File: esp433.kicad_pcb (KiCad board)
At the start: 2 copper layers, 47.1 x 72.6 mm, 35 parts, among them J1 USB_OTG, J2 CONN_01X03, Q1 MBT2222ADW1T1, SW1 SW_Push, U1 AP2127K-3.3, U2 IRM-02-5, U3 ESP-12E, U4 FT231XS

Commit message: Add rf circuit
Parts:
- added AE1: Antenna, esp433:W3127, F.Cu at (97.7, 130.3)
- added C3: 100n, Capacitors_SMD:C_0603, F.Cu at (102.1, 117.9)
- added C4: 220p, Capacitors_SMD:C_0603, F.Cu at (100.8, 117.9)
- added C5: 680p, Capacitors_SMD:C_0603, F.Cu at (99.6, 117.9)
- added C6: 12p, Capacitors_SMD:C_0603, F.Cu at (98.8, 125.2)
- added C7: 12p, Capacitors_SMD:C_0603, F.Cu at (97.3, 121.4)
- added C8: 100n, Capacitors_SMD:C_0603, F.Cu at (103.6, 124.5)
- added L2: 27nH, Inductors_SMD:L_0603, F.Cu at (98.0, 119.4)
- added L3: 15nH, Inductors_SMD:L_0603, F.Cu at (98.0, 123.4)
- added R6: R_Variable, Potentiometers:Potentiometer_Trimmer_Vishay_TS53YL, F.Cu at (108.2, 121.4)
- added U3: MAX7044, TO_SOT_Packages_SMD:SOT-23-8, F.Cu at (102.4, 121.4)
- added Y1: Crystal, Crystals:Crystal_HC49-U_Vertical, F.Cu at (117.3, 117.8)
- SW1: footprint Buttons_Switches_SMD:SW_SPST_PTS645 -> Buttons_Switches_SMD:SW_SPST_B3U-1000P
- moved SW1 37.5 mm to (135.6, 84.6), turned to 270 degrees
- moved D1 11.9 mm to (128.0, 120.4)
- moved J2 3.54 mm to (130.6, 129.3)
- renumbered C7 to C1, C2 to C10, C3 to C11, C4 to C12, C5 to C13, C6 to C14, C8 to C2, C1 to C9, R9 to R10, R10 to R11, R6 to R7, R7 to R9, U2 to U1, U1 to U2, U3 to U4, U4 to U5
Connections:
- U4 pad 5: (no net) -> /RF_CLK
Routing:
- net /RF_CLK: track 0.00 -> 36.9 mm, vias 0 -> 2
- net /RF_MOD: track 44.7 -> 73.9 mm, vias 0 -> 2
- net GND: track 26.8 -> 47.1 mm, vias 13 -> 21
- net +3V3: track 7.55 -> 24.9 mm, vias 3 -> 5
- net Net-(U3-Pad8): track 0.00 -> 16.0 mm
- net Net-(U3-Pad1): track 0.00 -> 15.8 mm
- net Net-(D1-Pad2): track 15.0 -> 27.9 mm
- net Net-(C3-Pad1): track 0.00 -> 10.2 mm
- net Net-(AE1-Pad1): track 0.00 -> 6.28 mm
- net Net-(C7-Pad1): track 0.00 -> 5.99 mm
- net +5V: track 45.2 -> 39.9 mm
- net /RESET: track 47.9 -> 49.8 mm, vias 4 -> 2

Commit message: Rearrange silk
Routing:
- net GND: track 47.1 -> 46.1 mm

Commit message: Rearrange filtering according to datasheet
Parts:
- moved C3 1.08 mm to (102.9, 117.1), turned to 180 degrees
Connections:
- C3 pad 1: Net-(C3-Pad1) -> +3V3
- C4 pad 1: Net-(C3-Pad1) -> Net-(C4-Pad1)
- C5 pad 1: Net-(C3-Pad1) -> Net-(C4-Pad1)
- L2 pad 1: Net-(C3-Pad1) -> Net-(C4-Pad1)
- R6 pad 2: Net-(C3-Pad1) -> Net-(C4-Pad1)
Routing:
- net +3V3: track 24.9 -> 14.0 mm
- net Net-(C4-Pad1): track 0.00 -> 10.2 mm
- net Net-(C3-Pad1): track 10.2 -> 0.00 mm
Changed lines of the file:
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@@
   (general
     (links 90)
-    (no_connects 0)
+    (no_connects 2)
     (area 90.679199 65.202999 137.920801 137.997001)
     (thickness 1.6)
     (drawings 20)
-    (tracks 319)
+    (tracks 317)
     (zones 0)
     (modules 47)
@@
   (net 23 /AC-L)
   (net 24 "Net-(AE1-Pad1)")
-  (net 25 "Net-(C3-Pad1)")
+  (net 25 "Net-(C4-Pad1)")
   (net 26 "Net-(C7-Pad1)")
   (net 27 "Net-(C9-Pad1)")
@@
     (add_net "Net-(AE1-Pad1)")
     (add_net "Net-(C14-Pad1)")
-    (add_net "Net-(C3-Pad1)")
+    (add_net "Net-(C4-Pad1)")
     (add_net "Net-(C7-Pad1)")
     (add_net "Net-(C9-Pad1)")
@@
   )
   (module Capacitors_SMD:C_0603 (layer F.Cu)
-    (at 102.108 117.856 90)
+    (at 102.87 117.094 180)
     (descr "Capacitor SMD 0603, reflow soldering, AVX (see smccp.pdf)")
     (tags "capacitor 0603")
     (attr smd)
-    (fp_text reference C3 (at 0.508 3.81 90) (layer F.SilkS)
-      (effects (font (size 1 1) (thickness 0.15)))
-    )
-    (fp_text value 100n (at 0 1.5 90) (layer F.Fab)
+    (fp_text reference C3 (at -2.286 0 180) (layer F.SilkS)
+      (effects (font (size 1 1) (thickness 0.15)))
+    )
+    (fp_text value 100n (at 0 1.5 180) (layer F.Fab)
+      (effects (font (size 1 1) (thickness 0.15)))
+    )
+    (fp_line (start 1.4 0.65) (end -1.4 0.65) (layer F.CrtYd) (width 0.05))
+    (fp_line (start 1.4 0.65) (end 1.4 -0.65) (layer F.CrtYd) (width 0.05))
+    (fp_line (start -1.4 -0.65) (end -1.4 0.65) (layer F.CrtYd) (width 0.05))
+    (fp_line (start -1.4 -0.65) (end 1.4 -0.65) (layer F.CrtYd) (width 0.05))
+    (fp_line (start 0.35 0.6) (end -0.35 0.6) (layer F.SilkS) (width 0.12))
+    (fp_line (start -0.35 -0.6) (end 0.35 -0.6) (layer F.SilkS) (width 0.12))
+    (fp_line (start -0.8 -0.4) (end 0.8 -0.4) (layer F.Fab) (width 0.1))
+    (fp_line (start 0.8 -0.4) (end 0.8 0.4) (layer F.Fab) (width 0.1))
+    (fp_line (start 0.8 0.4) (end -0.8 0.4) (layer F.Fab) (width 0.1))
+    (fp_line (start -0.8 0.4) (end -0.8 -0.4) (layer F.Fab) (width 0.1))
+    (fp_text user %R (at 0 0 180) (layer F.Fab)
+      (effects (font (size 0.3 0.3) (thickness 0.075)))
+    )
+    (pad 2 smd rect (at 0.75 0 180) (size 0.8 0.75) (layers F.Cu F.Paste F.Mask)
+      (net 1 GND))
+    (pad 1 smd rect (at -0.75 0 180) (size 0.8 0.75) (layers F.Cu F.Paste F.Mask)
+      (net 6 +3V3))
+    (model Capacitors_SMD.3dshapes/C_0603.wrl
+      (at (xyz 0 0 0))
+      (scale (xyz 1 1 1))
+      (rotate (xyz 0 0 0))
+    )
+  )
+  (module Capacitors_SMD:C_0603 (layer F.Cu)
+    (at 100.838 117.856 90)
+    (descr "Capacitor SMD 0603, reflow soldering, AVX (see smccp.pdf)")
+    (tags "capacitor 0603")
+    (attr smd)
+    (fp_text reference C4 (at -0.762 1.27 90) (layer F.SilkS)
+      (effects (font (size 1 1) (thickness 0.15)))
+    )
+    (fp_text value 220p (at 0 1.5 90) (layer F.Fab)
       (effects (font (size 1 1) (thickness 0.15)))
     )
@@
       (net 1 GND))
     (pad 1 smd rect (at -0.75 0 90) (size 0.8 0.75) (layers F.Cu F.Paste F.Mask)
-      (net 25 "Net-(C3-Pad1)"))
+      (net 25 "Net-(C4-Pad1)"))
     (model Capacitors_SMD.3dshapes/C_0603.wrl
       (at (xyz 0 0 0))
@@
   )
   (module Capacitors_SMD:C_0603 (layer F.Cu)
-    (at 100.838 117.856 90)
+    (at 99.568 117.856 90)
     (descr "Capacitor SMD 0603, reflow soldering, AVX (see smccp.pdf)")
     (tags "capacitor 0603")
     (attr smd)
-    (fp_text reference C4 (at 0.508 3.81 90) (layer F.SilkS)
-      (effects (font (size 1 1) (thickness 0.15)))
-    )
-    (fp_text value 220p (at 0 1.5 90) (layer F.Fab)
+    (fp_text reference C5 (at 0.508 -1.524 270) (layer F.SilkS)
+      (effects (font (size 1 1) (thickness 0.15)))
+    )
+    (fp_text value 680p (at 0 1.5 90) (layer F.Fab)
       (effects (font (size 1 1) (thickness 0.15)))
     )
@@
       (net 1 GND))
     (pad 1 smd rect (at -0.75 0 90) (size 0.8 0.75) (layers F.Cu F.Paste F.Mask)
-      (net 25 "Net-(C3-Pad1)"))
-    (model Capacitors_SMD.3dshapes/C_0603.wrl
-      (at (xyz 0 0 0))
-      (scale (xyz 1 1 1))
-      (rotate (xyz 0 0 0))
-    )
-  )
-  (module Capacitors_SMD:C_0603 (layer F.Cu)
-    (at 99.568 117.856 90)
-    (descr "Capacitor SMD 0603, reflow soldering, AVX (see smccp.pdf)")
-    (tags "capacitor 0603")
-    (attr smd)
-    (fp_text reference C5 (at 0.508 3.81 90) (layer F.SilkS)
-      (effects (font (size 1 1) (thickness 0.15)))
-    )
-    (fp_text value 680p (at 0 1.5 90) (layer F.Fab)
-      (effects (font (size 1 1) (thickness 0.15)))
-    )
-    (fp_line (start 1.4 0.65) (end -1.4 0.65) (layer F.CrtYd) (width 0.05))
-    (fp_line (start 1.4 0.65) (end 1.4 -0.65) (layer F.CrtYd) (width 0.05))
-    (fp_line (start -1.4 -0.65) (end -1.4 0.65) (layer F.CrtYd) (width 0.05))
-    (fp_line (start -1.4 -0.65) (end 1.4 -0.65) (layer F.CrtYd) (width 0.05))
-    (fp_line (start 0.35 0.6) (end -0.35 0.6) (layer F.SilkS) (width 0.12))
-    (fp_line (start -0.35 -0.6) (end 0.35 -0.6) (layer F.SilkS) (width 0.12))
-    (fp_line (start -0.8 -0.4) (end 0.8 -0.4) (layer F.Fab) (width 0.1))
-    (fp_line (start 0.8 -0.4) (end 0.8 0.4) (layer F.Fab) (width 0.1))
-    (fp_line (start 0.8 0.4) (end -0.8 0.4) (layer F.Fab) (width 0.1))
-    (fp_line (start -0.8 0.4) (end -0.8 -0.4) (layer F.Fab) (width 0.1))
-    (fp_text user %R (at 0 0 90) (layer F.Fab)
-      (effects (font (size 0.3 0.3) (thickness 0.075)))
-    )
-    (pad 2 smd rect (at 0.75 0 90) (size 0.8 0.75) (layers F.Cu F.Paste F.Mask)
-      (net 1 GND))
-    (pad 1 smd rect (at -0.75 0 90) (size 0.8 0.75) (layers F.Cu F.Paste F.Mask)
-      (net 25 "Net-(C3-Pad1)"))
+      (net 25 "Net-(C4-Pad1)"))
     (model Capacitors_SMD.3dshapes/C_0603.wrl
       (at (xyz 0 0 0))
@@
     (fp_line (start -0.5 -0.68) (end 0.5 -0.68) (layer F.SilkS) (width 0.12))
     (pad 1 smd rect (at -0.75 0 270) (size 0.5 0.9) (layers F.Cu F.Paste F.Mask)
-      (net 25 "Net-(C3-Pad1)"))
+      (net 25 "Net-(C4-Pad1)"))
     (pad 2 smd rect (at 0.75 0 270) (size 0.5 0.9) (layers F.Cu F.Paste F.Mask)
       (net 26 "Net-(C7-Pad1)"))
@@
       (net 6 +3V3))
     (pad 2 smd rect (at -2.75 0 270) (size 2 1.3) (layers F.Cu F.Mask)
-      (net 25 "Net-(C3-Pad1)"))
+      (net 25 "Net-(C4-Pad1)"))
     (pad 3 smd rect (at 2.75 1.15 270) (size 1.3 1.3) (layers F.Cu F.Mask))
     (model Potentiometers.3dshapes/Potentiometer_Trimmer_Vishay_TS53YL.wrl
@@
   (segment (start 125.222 120.396) (end 127.166 120.396) (width 0.508) (layer F.Cu) (net 5))
   (segment (start 121.158 116.332) (end 125.222 120.396) (width 0.508) (layer B.Cu) (net 5))
-  (segment (start 102.858 113.03) (end 102.596 113.03) (width 0.25) (layer F.Cu) (net 5))
-  (segment (start 102.907 124.46) (end 105.193 122.174) (width 0.25) (layer F.Cu) (net 6))
-  (segment (start 105.193 122.174) (end 113.284 122.174) (width 0.25) (layer F.Cu) (net 6))
-  (via (at 113.284 122.174) (size 0.6) (drill 0.4) (layers F.Cu B.Cu) (net 6))
-  (segment (start 109.354 124.118) (end 113.196 124.118) (width 0.34798) (layer F.Cu) (net 6))
-  (via (at 113.284 124.206) (size 0.6) (drill 0.4) (layers F.Cu B.Cu) (net 6))
-  (segment (start 113.196 124.118) (end 113.284 124.206) (width 0.34798) (layer F.Cu) (net 6))
+  (segment (start 102.907 124.46) (end 104.431 122.936) (width 0.25) (layer F.Cu) (net 6))
+  (segment (start 104.431 122.936) (end 105.156 122.936) (width 0.25) (layer F.Cu) (net 6))
+  (via (at 105.156 122.936) (size 0.6) (drill 0.4) (layers F.Cu B.Cu) (net 6))
+  (segment (start 103.62 117.094) (end 105.156 117.094) (width 0.34798) (layer F.Cu) (net 6))
+  (via (at 105.156 117.094) (size 0.6) (drill 0.4) (layers F.Cu B.Cu) (net 6))
   (segment (start 102.882 124.46) (end 102.907 124.46) (width 0.25) (layer F.Cu) (net 6))
   (segment (start 102.692 122.512) (end 102.692 124.27) (width 0.25) (layer F.Cu) (net 6))
@@
   (segment (start 98.044 124.194) (end 98.044 125.21) (width 0.25) (layer F.Cu) (net 24))
   (segment (start 98.044 125.21) (end 98.056 125.222) (width 0.25) (layer F.Cu) (net 24))
-  (segment (start 102.108 118.606) (end 108.192 118.606) (width 0.34798) (layer F.Cu) (net 25))
+  (segment (start 108.204 118.618) (end 100.85 118.618) (width 0.34798) (layer F.Cu) (net 25))
+  (segment (start 100.85 118.618) (end 100.838 118.606) (width 0.25) (layer F.Cu) (net 25))
   (segment (start 108.192 118.606) (end 108.204 118.618) (width 0.25) (layer F.Cu) (net 25))
-  (segment (start 100.838 118.606) (end 102.108 118.606) (width 0.34798) (layer F.Cu) (net 25))
   (segment (start 99.568 118.606) (end 100.838 118.606) (width 0.34798) (layer F.Cu) (net 25))
   (segment (start 98.044 118.63) (end 99.544 118.63) (width 0.34798) (layer F.Cu) (net 25))
@@
     (polygon
       (pts
-        (xy 112.776 91.694) (xy 137.922 91.694) (xy 137.922 125.984) (xy 112.776 125.984)
+        (xy 104.648 91.694) (xy 137.922 91.694) (xy 137.922 125.984) (xy 104.648 125.984)
       )
     )

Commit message: Correct hot/neutral labeling on power input
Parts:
- moved MK1 12.7 mm to (114.3, 73.7)
- moved MK2 12.4 mm to (101.9, 73.7)
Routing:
- net /AC-L: track 14.1 -> 25.2 mm
- net /AC-N: track 13.1 -> 16.9 mm
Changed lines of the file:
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@@
     (thickness 1.6)
     (drawings 20)
-    (tracks 317)
+    (tracks 319)
     (zones 0)
     (modules 47)
@@
     (47 F.CrtYd user)
     (48 B.Fab user)
-    (49 F.Fab user hide)
+    (49 F.Fab user)
   )
   (setup
@@
   )
   (module Wire_Pads:SolderWirePad_single_2mmDrill (layer F.Cu)
-    (at 101.6 73.66)
+    (at 114.3 73.66)
     (fp_text reference MK1 (at 0 -3.81) (layer F.SilkS)
       (effects (font (size 1 1) (thickness 0.15)))
@@
   )
   (module Wire_Pads:SolderWirePad_single_2mmDrill (layer F.Cu)
-    (at 114.3 73.66)
+    (at 101.854 73.66)
     (fp_text reference MK2 (at 0 -3.81) (layer F.SilkS)
       (effects (font (size 1 1) (thickness 0.15)))
@@
   (segment (start 115.263145 112.021891) (end 115.063145 112.021891) (width 0.25) (layer F.Cu) (net 21))
   (segment (start 115.063145 112.021891) (end 114.374145 111.332891) (width 0.25) (layer F.Cu) (net 21))
-  (segment (start 114.3 73.66) (end 114.3 80.926) (width 1.27) (layer F.Cu) (net 22))
-  (segment (start 114.3 80.926) (end 110.196 85.03) (width 1.27) (layer F.Cu) (net 22))
-  (segment (start 101.6 73.66) (end 101.6 78.426) (width 1.27) (layer F.Cu) (net 23))
-  (segment (start 101.6 78.426) (end 94.996 85.03) (width 1.27) (layer F.Cu) (net 23))
+  (segment (start 106.62 85.03) (end 101.854 80.264) (width 1.27) (layer B.Cu) (net 22))
+  (segment (start 110.196 85.03) (end 106.62 85.03) (width 1.27) (layer B.Cu) (net 22))
+  (segment (start 101.854 80.264) (end 101.854 73.66) (width 1.27) (layer B.Cu) (net 22))
+  (segment (start 94.996 85.03) (end 104.962 85.03) (width 1.27) (layer F.Cu) (net 23))
+  (segment (start 104.962 85.03) (end 114.3 75.692) (width 1.27) (layer F.Cu) (net 23))
+  (segment (start 114.3 75.692) (end 114.3 73.66) (width 0.25) (layer F.Cu) (net 23))
   (segment (start 98.056 125.222) (end 98.056 129.909) (width 0.34798) (layer F.Cu) (net 24))
   (segment (start 98.056 129.909) (end 97.663 130.302) (width 0.25) (layer F.Cu) (net 24))

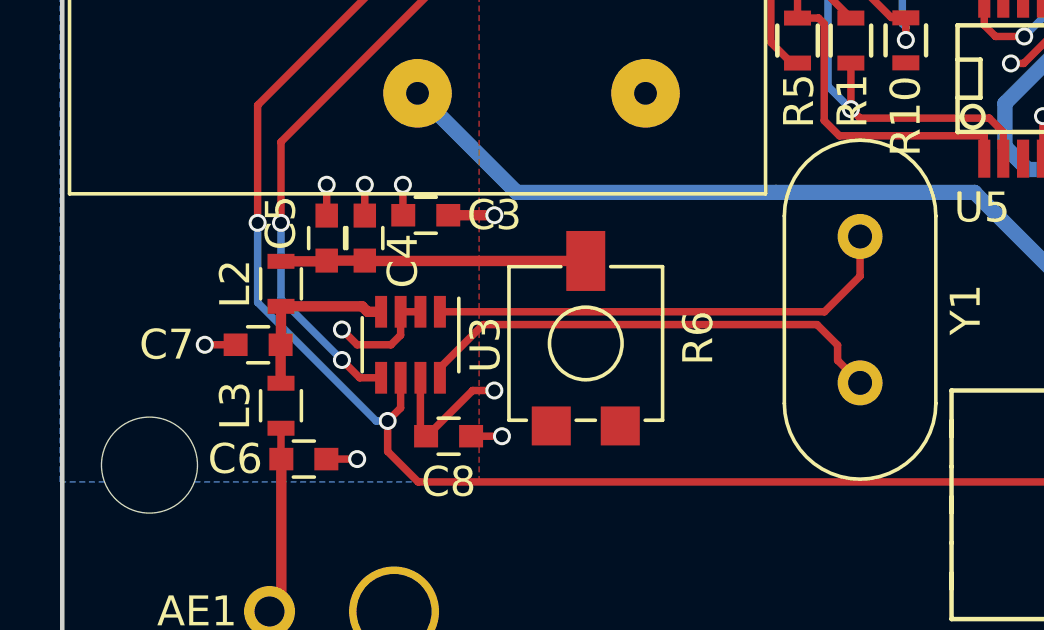
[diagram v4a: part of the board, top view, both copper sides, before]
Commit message: Rework to fix oscillator and antenna circuit
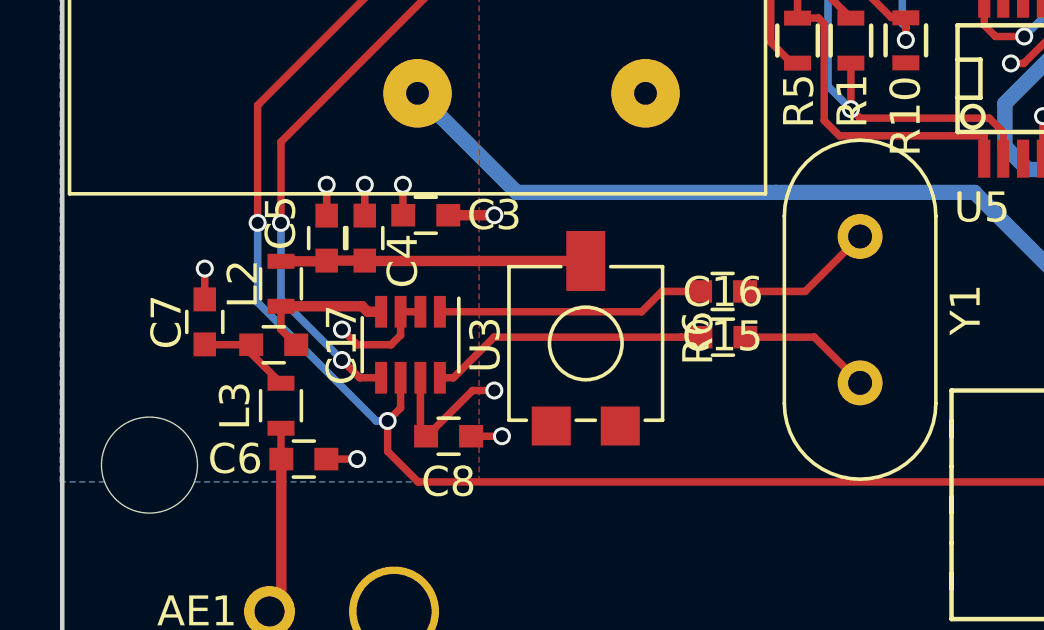
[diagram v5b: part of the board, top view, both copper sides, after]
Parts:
- added C15: 12p, Capacitors_SMD:C_0603, F.Cu at (112.8, 119.6)
- added C16: 12p, Capacitors_SMD:C_0603, F.Cu at (112.8, 121.2)
- added C17: 15p, Capacitors_SMD:C_0603, F.Cu at (97.8, 121.4)
- moved C7 1.93 mm to (95.5, 120.7), turned to 90 degrees
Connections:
- C7 pad 1: Net-(C7-Pad1) -> Net-(C17-Pad2)
- L2 pad 2: Net-(C7-Pad1) -> Net-(C17-Pad1)
- L3 pad 1: Net-(C7-Pad1) -> Net-(C17-Pad2)
- U3 pad 1: Net-(U3-Pad1) -> Net-(C15-Pad2)
- U3 pad 4: Net-(C7-Pad1) -> Net-(C17-Pad1)
- U3 pad 8: Net-(U3-Pad8) -> Net-(C16-Pad1)
- Y1 pad 1: Net-(U3-Pad1) -> Net-(C15-Pad1)
- Y1 pad 2: Net-(U3-Pad8) -> Net-(C16-Pad2)
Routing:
- net Net-(U3-Pad8): track 16.0 -> 0.00 mm
- net Net-(U3-Pad1): track 15.8 -> 0.00 mm
- net Net-(C16-Pad1): track 0.00 -> 9.57 mm
- net Net-(C15-Pad2): track 0.00 -> 8.95 mm
- net Net-(C7-Pad1): track 5.99 -> 0.00 mm
- net Net-(C17-Pad1): track 0.00 -> 4.91 mm
- net Net-(C15-Pad1): track 0.00 -> 4.59 mm
- net Net-(C16-Pad2): track 0.00 -> 4.45 mm
- net Net-(C17-Pad2): track 0.00 -> 3.26 mm
